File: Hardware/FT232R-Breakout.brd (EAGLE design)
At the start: 30.5 x 20.3 mm, 20 parts, among them U1 FT232R

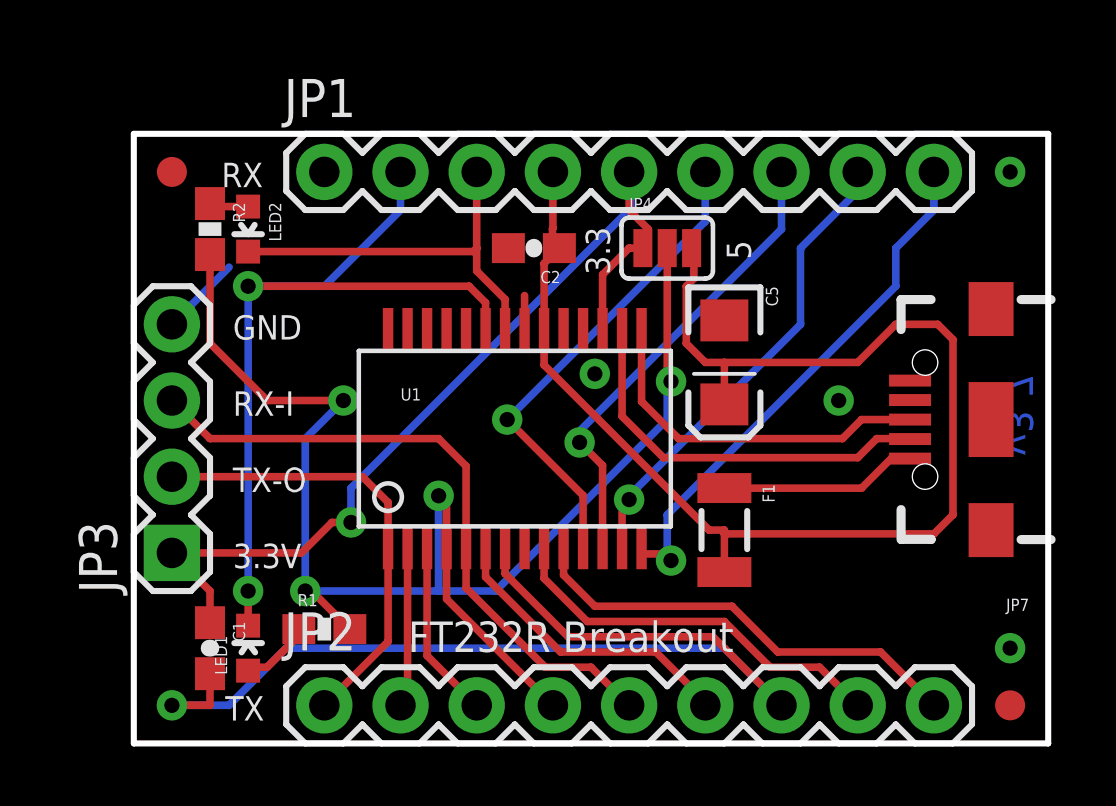
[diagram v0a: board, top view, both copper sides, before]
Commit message: Adding SMD switch for 3.3V/ 5V selection
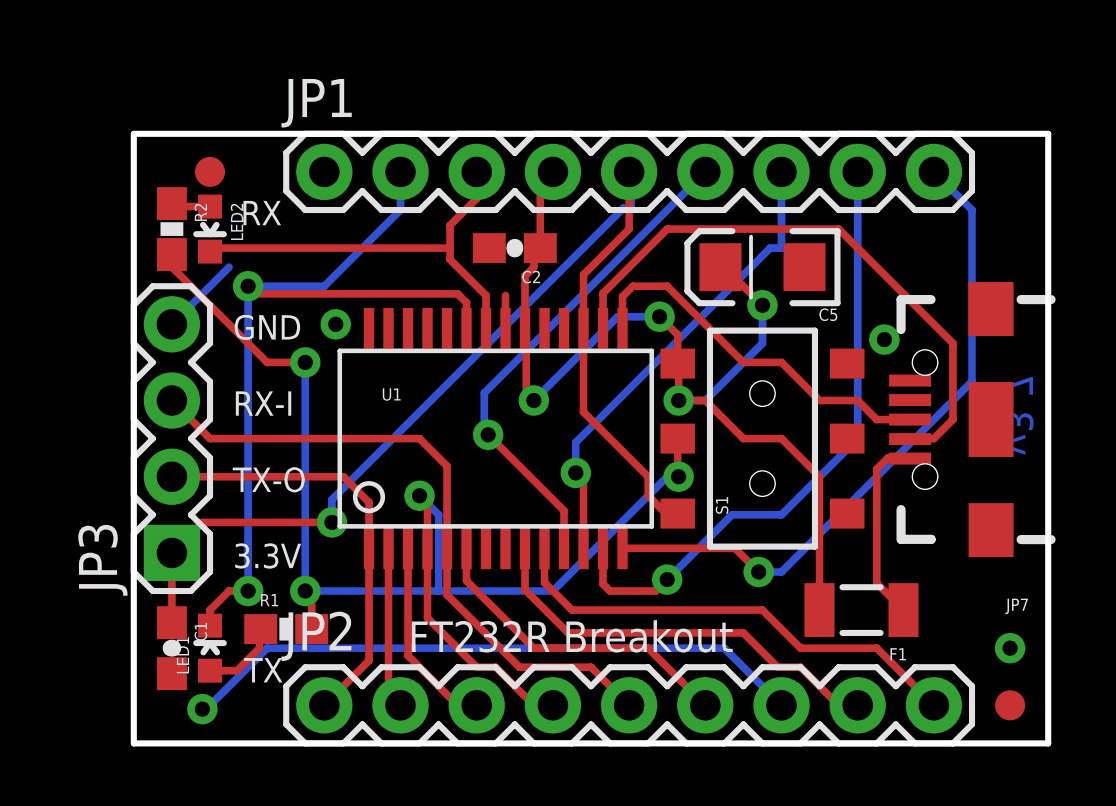
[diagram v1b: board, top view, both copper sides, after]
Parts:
- removed JP4: IO Select, SparkFun-Passives:SJ_3_PASTE1&2
- added S1: (no value), SparkFun-Electromechanical:AYZ0202
- moved F1 5.29 mm to (25.5, 5.71), turned to 180 degrees
- moved C5 3.42 mm to (22.2, 17.1), turned to 180 degrees
- moved R1 1.27 mm to (6.35, 5.08)
- moved C1 1.27 mm to (2.54, 4.45)
- moved JP6 1.27 mm to (3.81, 20.3)
- moved LED1 1.27 mm to (3.81, 4.45)
- moved LED2 1.27 mm to (3.81, 18.4)
- moved R2 1.27 mm to (2.54, 18.4)
- moved C2 0.63 mm to (14.0, 17.8)
- moved U1 0.63 mm to (13.3, 11.4)
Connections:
- net 3.3V: now also S1.1; no longer JP4.1
- net VCC: now also S1.3; no longer JP4.3
- net VCCIO: now also S1.2; no longer JP4.2
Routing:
- net GND: track 40.8 -> 25.1 mm, vias 5 -> 4
- net VCC: track 44.8 -> 33.5 mm, vias 0 -> 4
- net 3.3V: track 31.5 -> 37.8 mm
- net USB_D-: track 13.4 -> 19.6 mm
- net VCCIO: track 49.1 -> 43.6 mm
- net TXDEN: track 15.8 -> 20.8 mm
- net PWREN: track 18.0 -> 22.1 mm
- net TXD: track 15.2 -> 14.3 mm
- net DSR: track 13.2 -> 14.1 mm
- net RXLED: track 13.3 -> 14.1 mm
- net DCD: track 15.0 -> 15.8 mm
- net RI: track 10.1 -> 10.9 mm
- net RTS: track 5.92 -> 6.55 mm
- net USB_D+: track 12.1 -> 12.6 mm
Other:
- board text removed: "3.3"
- board text removed: "5"
